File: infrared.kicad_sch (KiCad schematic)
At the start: 0 parts

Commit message: add TSOP75338TR library
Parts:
- added IC1: TSOP75338TR, TSOP75338TR:TSOP75338TR, symbol TSOP75338TR:TSOP75338TR
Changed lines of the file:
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@@
 	(generator_version "9.0")
 	(paper "A4")
+	(symbol
+		(lib_id "TSOP75338TR:TSOP75338TR")
+		(at 87.63 68.58 0)
+		(unit 1)
+		(exclude_from_sim no)
+		(in_bom yes)
+		(on_board yes)
+		(dnp no)
+		(fields_autoplaced yes)
+		(property "Reference" "IC1"
+			(at 109.22 71.1199 0)
+			(effects
+				(font
+					(size 1.27 1.27)
+				)
+				(justify left)
+			)
+		)
+		(property "Value" "TSOP75338TR"
+			(at 109.22 73.6599 0)
+			(effects
+				(font
+					(size 1.27 1.27)
+				)
+				(justify left)
+			)
+		)
+		(property "Footprint" "TSOP75338TR:TSOP75338TR"
+			(at 109.22 163.5 0)
+			(effects
+				(font
+					(size 1.27 1.27)
+				)
+				(justify left top)
+				(hide yes)
+			)
+		)
+		(property "Datasheet" "http://www.vishay.com/docs/82495/tsop753.pdf"
+			(at 109.22 263.5 0)
+			(effects
+				(font
+					(size 1.27 1.27)
+				)
+				(justify left top)
+				(hide yes)
+			)
+		)
+		(property "Description" "Vishay TSOP75338TR, 38kHz IR Receiver, 950nm +/-50 , 45m Range, 2.5V - 5V, SMT, 6.8 x 3 x 3.2mm"
+			(at 87.63 68.58 0)
+			(effects
+				(font
+					(size 1.27 1.27)
+				)
+				(hide yes)
+			)
+		)
+		(property "Height" "3.35"
+			(at 109.22 463.5 0)
+			(effects
+				(font
+					(size 1.27 1.27)
+				)
+				(justify left top)
+				(hide yes)
+			)
+		)
+		(property "Manufacturer_Name" "Vishay"
+			(at 109.22 563.5 0)
+			(effects
+				(font
+					(size 1.27 1.27)
+				)
+				(justify left top)
+				(hide yes)
+			)
+		)
+		(property "Manufacturer_Part_Number" "TSOP75338TR"
+			(at 109.22 663.5 0)
+			(effects
+				(font
+					(size 1.27 1.27)
+				)
+				(justify left top)
+				(hide yes)
+			)
+		)
+		(property "Mouser Part Number" "78-TSOP75338TR"
+			(at 109.22 763.5 0)
+			(effects
+				(font
+					(size 1.27 1.27)
+				)
+				(justify left top)
+				(hide yes)
+			)
+		)
+		(property "Mouser Price/Stock" "https://www.mouser.co.uk/ProductDetail/Vishay-Semiconductors/TSOP75338TR?qs=OZzrG8p9eNh0IrZXKXgo8Q%3D%3D"
+			(at 109.22 863.5 0)
+			(effects
+				(font
+					(size 1.27 1.27)
+				)
+				(justify left top)
+				(hide yes)
+			)
+		)
+		(property "Arrow Part Number" "TSOP75338TR"
+			(at 109.22 963.5 0)
+			(effects
+				(font
+					(size 1.27 1.27)
+				)
+				(justify left top)
+				(hide yes)
+			)
+		)
+		(property "Arrow Price/Stock" "https://www.arrow.com/en/products/tsop75338tr/vishay?utm_currency=USD&region=nac"
+			(at 109.22 1063.5 0)
+			(effects
+				(font
+					(size 1.27 1.27)
+				)
+				(justify left top)
+				(hide yes)
+			)
+		)
+		(pin "2"
+		)
+		(pin "4"
+		)
+		(pin "3"
+		)
+		(pin "1"
+		)
+		(instances
+			(project ""
+				(path "/3130e1f2-bde1-4b12-bd54-0e1e50bd36da/4b0b0d5d-6833-4670-bedb-8ac2688b21e7"
+					(reference "IC1")
+					(unit 1)
+				)
+			)
+		)
+	)
 )

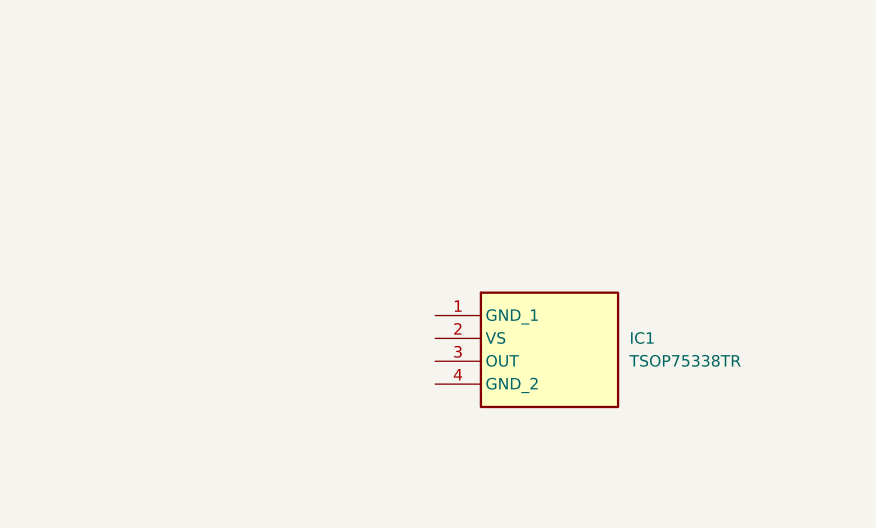
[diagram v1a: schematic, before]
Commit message: component placement inside schematic
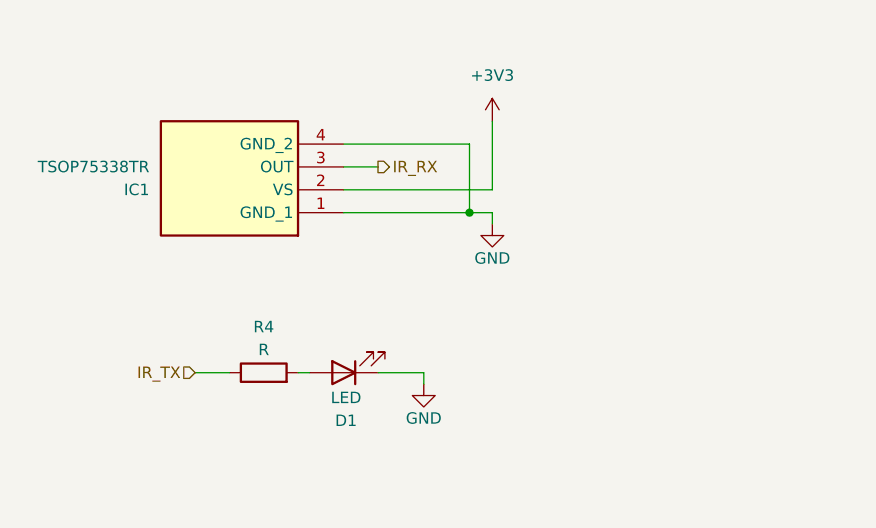
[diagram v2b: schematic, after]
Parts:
- added D1: LED, symbol Device:LED
- added R4: R, symbol Device:R
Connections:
- net GND: now reaches IC1.1 (GND_1)
- net GND: now also IC1.4 (GND_2), D1.1 (K)
- net +3V3: now reaches IC1.2 (VS)
- net IR_RX: now reaches IC1.3 (OUT)
- new net: D1.2 (A), R4.2
- new net IR_TX: R4.1
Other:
- moved on the sheet: IC1

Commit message: add external gpio connector
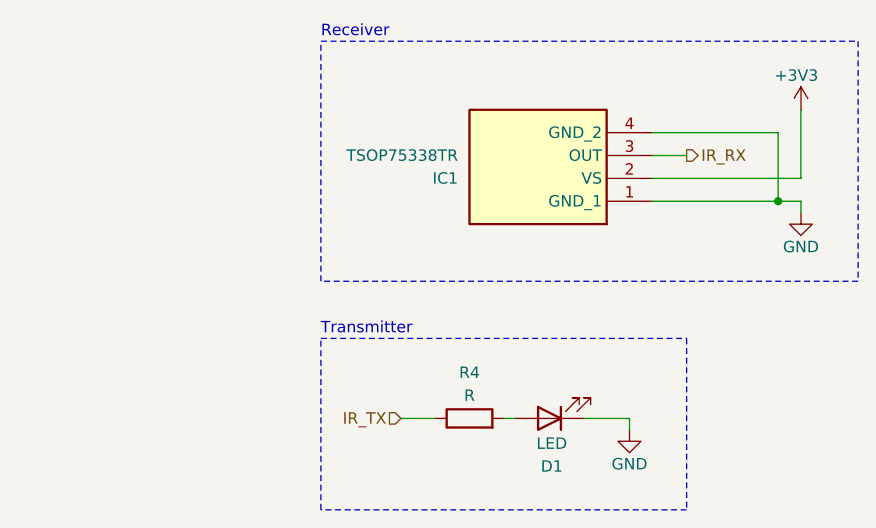
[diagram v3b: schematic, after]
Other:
- note added: "Receiver"
- note added: "Transmitter"
- moved on the sheet: D1, IC1, R4

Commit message: set initial component footprints
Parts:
- R11: renamed from R4; footprint (none) -> Resistor_SMD:R_0603_1608Metric
- renumbered D1 to D4, IC1 to IC2
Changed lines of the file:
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@@
 		(on_board yes)
 		(dnp no)
-		(property "Reference" "D1"
+		(property "Reference" "D4"
 			(at 100.584 85.344 0)
 			(effects
@@
 			(project ""
 				(path "/3130e1f2-bde1-4b12-bd54-0e1e50bd36da/4b0b0d5d-6833-4670-bedb-8ac2688b21e7"
-					(reference "D1")
+					(reference "D4")
 					(unit 1)
 				)
@@
 		(on_board yes)
 		(dnp no)
-		(property "Reference" "R4"
+		(property "Reference" "R11"
 			(at 91.44 74.93 90)
 			(effects
@@
 			)
 		)
-		(property "Footprint" ""
+		(property "Footprint" "Resistor_SMD:R_0603_1608Metric"
 			(at 91.44 81.788 90)
 			(effects
@@
 			(project ""
 				(path "/3130e1f2-bde1-4b12-bd54-0e1e50bd36da/4b0b0d5d-6833-4670-bedb-8ac2688b21e7"
-					(reference "R4")
+					(reference "R11")
 					(unit 1)
 				)
@@
 		(dnp no)
 		(fields_autoplaced yes)
-		(property "Reference" "IC1"
+		(property "Reference" "IC2"
 			(at 90.17 53.3401 0)
 			(effects
@@
 			(project ""
 				(path "/3130e1f2-bde1-4b12-bd54-0e1e50bd36da/4b0b0d5d-6833-4670-bedb-8ac2688b21e7"
-					(reference "IC1")
+					(reference "IC2")
 					(unit 1)
 				)
@@
 		(on_board yes)
 		(dnp no)
-		(property "Reference" "#PWR025"
+		(property "Reference" "#PWR017"
 			(at 128.27 49.53 0)
 			(effects
@@
 			(project ""
 				(path "/3130e1f2-bde1-4b12-bd54-0e1e50bd36da/4b0b0d5d-6833-4670-bedb-8ac2688b21e7"
-					(reference "#PWR025")
+					(reference "#PWR017")
 					(unit 1)
 				)
@@
 		(on_board yes)
 		(dnp no)
-		(property "Reference" "#PWR026"
+		(property "Reference" "#PWR018"
 			(at 128.27 63.5 0)
 			(effects
@@
 			(project ""
 				(path "/3130e1f2-bde1-4b12-bd54-0e1e50bd36da/4b0b0d5d-6833-4670-bedb-8ac2688b21e7"
-					(reference "#PWR026")
+					(reference "#PWR018")
 					(unit 1)
 				)
@@
 		(on_board yes)
 		(dnp no)
-		(property "Reference" "#PWR027"
+		(property "Reference" "#PWR016"
 			(at 109.22 87.63 0)
 			(effects
@@
 			(project ""
 				(path "/3130e1f2-bde1-4b12-bd54-0e1e50bd36da/4b0b0d5d-6833-4670-bedb-8ac2688b21e7"
-					(reference "#PWR027")
-					(unit 1)
-				)
+					(reference "#PWR016")
+					(unit 1)
+				)

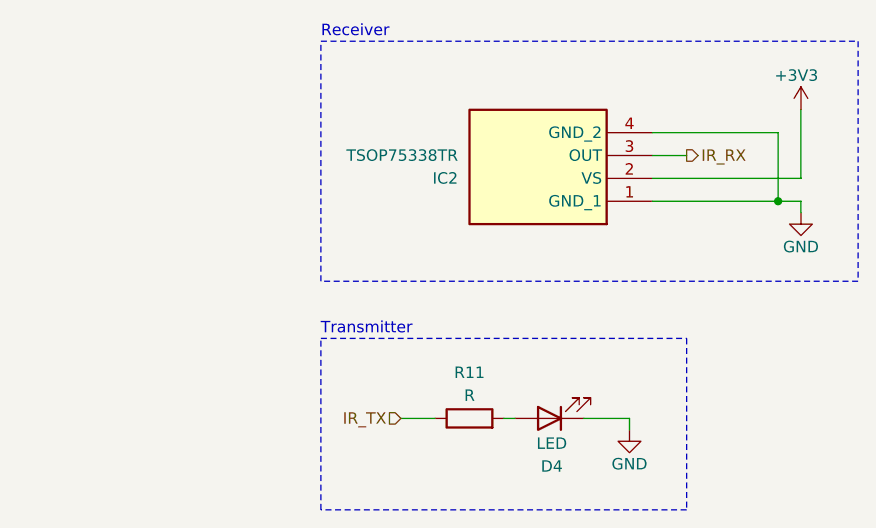
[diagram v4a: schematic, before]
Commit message: Add footprints
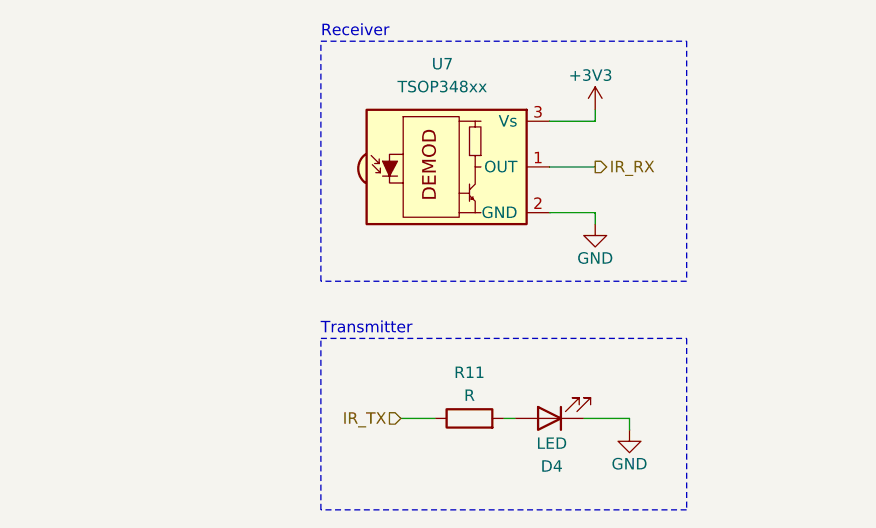
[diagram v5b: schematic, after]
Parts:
- removed IC2: TSOP75338TR, TSOP75338TR:TSOP75338TR, symbol TSOP75338TR:TSOP75338TR
- added U7: TSOP348xx, OptoDevice:Vishay_MOLD-3Pin, symbol Interface_Optical:TSOP348xx
- D4: footprint (none) -> LED_THT:LED_D3.0mm_Horizontal_O1.27mm_Z2.0mm
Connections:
- net +3V3: now also U7.3 (Vs)
- net GND: now also U7.2 (GND)
- net IR_RX: now also U7.1 (OUT)
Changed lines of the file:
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@@
 	(rectangle
 		(start 74.93 38.1)
-		(end 134.62 64.77)
+		(end 115.57 64.77)
 		(stroke
 			(width 0)
@@
 		)
 	)
-	(junction
-		(at 125.73 55.88)
-		(diameter 0)
-		(color 0 0 0 0)
-	)
 	(wire
 		(pts
@@
 	(wire
 		(pts
-			(xy 128.27 45.72) (xy 128.27 53.34)
-		)
-		(stroke
-			(width 0)
-			(type default)
-		)
-	)
-	(wire
-		(pts
-			(xy 125.73 48.26) (xy 111.76 48.26)
-		)
-		(stroke
-			(width 0)
-			(type default)
-		)
-	)
-	(wire
-		(pts
-			(xy 128.27 55.88) (xy 128.27 57.15)
+			(xy 105.41 45.72) (xy 105.41 46.99)
+		)
+		(stroke
+			(width 0)
+			(type default)
+		)
+	)
+	(wire
+		(pts
+			(xy 100.33 52.07) (xy 105.41 52.07)
+		)
+		(stroke
+			(width 0)
+			(type default)
+		)
+	)
+	(wire
+		(pts
+			(xy 105.41 57.15) (xy 105.41 58.42)
 		)
 		(stroke
@@
 	(wire
 		(pts
-			(xy 125.73 55.88) (xy 111.76 55.88)
-		)
-		(stroke
-			(width 0)
-			(type default)
-		)
-	)
-	(wire
-		(pts
-			(xy 128.27 53.34) (xy 111.76 53.34)
-		)
-		(stroke
-			(width 0)
-			(type default)
-		)
-	)
-	(wire
-		(pts
-			(xy 111.76 50.8) (xy 115.57 50.8)
-		)
-		(stroke
-			(width 0)
-			(type default)
-		)
-	)
-	(wire
-		(pts
-			(xy 125.73 48.26) (xy 125.73 55.88)
-		)
-		(stroke
-			(width 0)
-			(type default)
-		)
-	)
-	(wire
-		(pts
-			(xy 128.27 55.88) (xy 125.73 55.88)
+			(xy 100.33 57.15) (xy 105.41 57.15)
+		)
+		(stroke
+			(width 0)
+			(type default)
+		)
+	)
+	(wire
+		(pts
+			(xy 105.41 46.99) (xy 100.33 46.99)
 		)
 		(stroke
@@
 	(hierarchical_label "IR_RX"
 		(shape output)
-		(at 115.57 50.8 0)
+		(at 105.41 52.07 0)
 		(effects
 			(font
@@
 			)
 		)
-		(property "Footprint" ""
+		(property "Footprint" "LED_THT:LED_D3.0mm_Horizontal_O1.27mm_Z2.0mm"
 			(at 100.33 80.01 0)
 			(effects
@@
 	)
 	(symbol
+		(lib_id "Interface_Optical:TSOP348xx")
+		(at 90.17 52.07 0)
+		(unit 1)
+		(exclude_from_sim no)
+		(in_bom yes)
+		(on_board yes)
+		(dnp no)
+		(fields_autoplaced yes)
+		(property "Reference" "U7"
+			(at 88.435 40.64 0)
+			(effects
+				(font
+					(size 1.27 1.27)
+				)
+			)
+		)
+		(property "Value" "TSOP348xx"
+			(at 88.435 43.18 0)
+			(effects
+				(font
+					(size 1.27 1.27)
+				)
+			)
+		)
+		(property "Footprint" "OptoDevice:Vishay_MOLD-3Pin"
+			(at 88.9 61.595 0)
+			(effects
+				(font
+					(size 1.27 1.27)
+				)
+				(hide yes)
+			)
+		)
+		(property "Datasheet" "https://www.vishay.com/docs/82489/tsop322.pdf"
+			(at 106.68 44.45 0)
+			(effects
+				(font
+					(size 1.27 1.27)
+				)
+				(hide yes)
+			)
+		)
+		(property "Description" "IR Receiver Modules for Remote Control Systems"
+			(at 90.17 52.07 0)
+			(effects
+				(font
+					(size 1.27 1.27)
+				)
+				(hide yes)
+			)
+		)
+		(pin "2"
+		)
+		(pin "3"
+		)
+		(pin "1"
+		)
+		(instances
+			(project ""
+				(path "/3130e1f2-bde1-4b12-bd54-0e1e50bd36da/4b0b0d5d-6833-4670-bedb-8ac2688b21e7"
+					(reference "U7")
+					(unit 1)
+				)
+			)
+		)
+	)
+	(symbol
 		(lib_id "Device:R")
 		(at 91.44 80.01 90)
@@
 	)
 	(symbol
-		(lib_id "TSOP75338TR:TSOP75338TR")
-		(at 111.76 55.88 180)
-		(unit 1)
-		(exclude_from_sim no)
-		(in_bom yes)
-		(on_board yes)
-		(dnp no)
-		(fields_autoplaced yes)
-		(property "Reference" "IC2"
-			(at 90.17 53.3401 0)
-			(effects
-				(font
-					(size 1.27 1.27)
-				)
-				(justify left)
-			)
-		)
-		(property "Value" "TSOP75338TR"
-			(at 90.17 50.8001 0)
-			(effects
-				(font
-					(size 1.27 1.27)
-				)
-				(justify left)
-			)
-		)
-		(property "Footprint" "TSOP75338TR:TSOP75338TR"
-			(at 90.17 -39.04 0)
-			(effects
-				(font
-					(size 1.27 1.27)
-				)
-				(justify left top)
-				(hide yes)
-			)
-		)
-		(property "Datasheet" "http://www.vishay.com/docs/82495/tsop753.pdf"
-			(at 90.17 -139.04 0)
-			(effects
-				(font
-					(size 1.27 1.27)
-				)
-				(justify left top)
-				(hide yes)
-			)
-		)
-		(property "Description" "Vishay TSOP75338TR, 38kHz IR Receiver, 950nm +/-50 , 45m Range, 2.5V - 5V, SMT, 6.8 x 3 x 3.2mm"
-			(at 111.76 55.88 0)
-			(effects
-				(font
-					(size 1.27 1.27)
-				)
-				(hide yes)
-			)
-		)
-		(property "Height" "3.35"
-			(at 90.17 -339.04 0)
-			(effects
-				(font
-					(size 1.27 1.27)
-				)
-				(justify left top)
-				(hide yes)
-			)
-		)
-		(property "Manufacturer_Name" "Vishay"
-			(at 90.17 -439.04 0)
-			(effects
-				(font
-					(size 1.27 1.27)
-				)
-				(justify left top)
-				(hide yes)
-			)
-		)
-		(property "Manufacturer_Part_Number" "TSOP75338TR"
-			(at 90.17 -539.04 0)
-			(effects
-				(font
-					(size 1.27 1.27)
-				)
-				(justify left top)
-				(hide yes)
-			)
-		)
-		(property "Mouser Part Number" "78-TSOP75338TR"
-			(at 90.17 -639.04 0)
-			(effects
-				(font
-					(size 1.27 1.27)
-				)
-				(justify left top)
-				(hide yes)
-			)
-		)
-		(property "Mouser Price/Stock" "https://www.mouser.co.uk/ProductDetail/Vishay-Semiconductors/TSOP75338TR?qs=OZzrG8p9eNh0IrZXKXgo8Q%3D%3D"
-			(at 90.17 -739.04 0)
-			(effects
-				(font
-					(size 1.27 1.27)
-				)
-				(justify left top)
-				(hide yes)
-			)
-		)
-		(property "Arrow Part Number" "TSOP75338TR"
-			(at 90.17 -839.04 0)
-			(effects
-				(font
-					(size 1.27 1.27)
-				)
-				(justify left top)
-				(hide yes)
-			)
-		)
-		(property "Arrow Price/Stock" "https://www.arrow.com/en/products/tsop75338tr/vishay?utm_currency=USD&region=nac"
-			(at 90.17 -939.04 0)
-			(effects
-				(font
-					(size 1.27 1.27)
-				)
-				(justify left top)
-				(hide yes)
-			)
-		)
-		(pin "2"
-		)
-		(pin "4"
-		)
-		(pin "3"
-		)
-		(pin "1"
-		)
-		(instances
-			(project ""
-				(path "/3130e1f2-bde1-4b12-bd54-0e1e50bd36da/4b0b0d5d-6833-4670-bedb-8ac2688b21e7"
-					(reference "IC2")
-					(unit 1)
-				)
-			)
-		)
-	)
-	(symbol
 		(lib_id "power:+3V3")
-		(at 128.27 45.72 0)
+		(at 105.41 45.72 0)
 		(unit 1)
 		(exclude_from_sim no)
@@
 		(dnp no)
 		(property "Reference" "#PWR017"
-			(at 128.27 49.53 0)
+			(at 105.41 49.53 0)
 			(effects
 				(font
@@
 		)
 		(property "Value" "+3V3"
-			(at 127.762 41.91 0)
+			(at 104.902 41.91 0)
 			(effects
 				(font
@@
 		)
 		(property "Footprint" ""
-			(at 128.27 45.72 0)
+			(at 105.41 45.72 0)
 			(effects
 				(font
@@
 		)
 		(property "Datasheet" ""
-			(at 128.27 45.72 0)
+			(at 105.41 45.72 0)
 			(effects
 				(font
@@
 		)
 		(property "Description" "Power symbol creates a global label with name \"+3V3\""
-			(at 128.27 45.72 0)
+			(at 105.41 45.72 0)
 			(effects
 				(font
@@
 	(symbol
 		(lib_id "power:GND")
-		(at 128.27 57.15 0)
+		(at 105.41 58.42 0)
 		(unit 1)
 		(exclude_from_sim no)
@@
 		(dnp no)
 		(property "Reference" "#PWR018"
-			(at 128.27 63.5 0)
+			(at 105.41 64.77 0)
 			(effects
 				(font
@@
 		)
 		(property "Value" "GND"
-			(at 128.27 60.96 0)
+			(at 105.41 62.23 0)
 			(effects
 				(font
@@
 		)
 		(property "Footprint" ""
-			(at 128.27 57.15 0)
+			(at 105.41 58.42 0)
 			(effects
 				(font
@@
 		)
 		(property "Datasheet" ""
-			(at 128.27 57.15 0)
+			(at 105.41 58.42 0)
 			(effects
 				(font
@@
 		)
 		(property "Description" "Power symbol creates a global label with name \"GND\" , ground"
-			(at 128.27 57.15 0)
-			(effects
-				(font
+			(at 105.41 58.42 0)
+			(effects
+				(font

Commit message: modify ios
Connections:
- net +3V3: now also D4.2 (A)
- net GND: no longer D4.1 (K)
- net at R11.2: now also D4.1 (K); no longer D4.2 (A)
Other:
- moved on the sheet: D4
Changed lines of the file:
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@@
-	(wire
-		(pts
-			(xy 109.22 80.01) (xy 109.22 81.28)
-		)
-		(stroke
-			(width 0)
-			(type default)
-		)
-	)
 	(wire
 		(pts
@@
 		(pts
 			(xy 105.41 46.99) (xy 100.33 46.99)
+		)
+		(stroke
+			(width 0)
+			(type default)
+		)
+	)
+	(wire
+		(pts
+			(xy 109.22 78.74) (xy 109.22 80.01)
 		)
 		(stroke
@@
 	(symbol
 		(lib_id "Device:LED")
-		(at 100.33 80.01 180)
+		(at 100.33 80.01 0)
 		(unit 1)
 		(exclude_from_sim no)
@@
 		(dnp no)
 		(property "Reference" "D4"
-			(at 100.584 85.344 0)
+			(at 100.076 74.676 0)
 			(effects
 				(font
@@
 		)
 		(property "Value" "LED"
-			(at 100.584 82.804 0)
+			(at 100.076 77.216 0)
 			(effects
 				(font
@@
 	(symbol
 		(lib_id "power:+3V3")
+		(at 109.22 78.74 0)
+		(unit 1)
+		(exclude_from_sim no)
+		(in_bom yes)
+		(on_board yes)
+		(dnp no)
+		(fields_autoplaced yes)
+		(property "Reference" "#PWR016"
+			(at 109.22 82.55 0)
+			(effects
+				(font
+					(size 1.27 1.27)
+				)
+				(hide yes)
+			)
+		)
+		(property "Value" "+3V3"
+			(at 109.22 73.66 0)
+			(effects
+				(font
+					(size 1.27 1.27)
+				)
+			)
+		)
+		(property "Footprint" ""
+			(at 109.22 78.74 0)
+			(effects
+				(font
+					(size 1.27 1.27)
+				)
+				(hide yes)
+			)
+		)
+		(property "Datasheet" ""
+			(at 109.22 78.74 0)
+			(effects
+				(font
+					(size 1.27 1.27)
+				)
+				(hide yes)
+			)
+		)
+		(property "Description" "Power symbol creates a global label with name \"+3V3\""
+			(at 109.22 78.74 0)
+			(effects
+				(font
+					(size 1.27 1.27)
+				)
+				(hide yes)
+			)
+		)
+		(pin "1"
+		)
+		(instances
+			(project ""
+				(path "/3130e1f2-bde1-4b12-bd54-0e1e50bd36da/4b0b0d5d-6833-4670-bedb-8ac2688b21e7"
+					(reference "#PWR016")
+					(unit 1)
+				)
+			)
+		)
+	)
+	(symbol
+		(lib_id "power:+3V3")
 		(at 105.41 45.72 0)
 		(unit 1)
@@
 					(unit 1)
 				)
-			)
-		)
-	)
-	(symbol
-		(lib_id "power:GND")
-		(at 109.22 81.28 0)
-		(unit 1)
-		(exclude_from_sim no)
-		(in_bom yes)
-		(on_board yes)
-		(dnp no)
-		(property "Reference" "#PWR016"
-			(at 109.22 87.63 0)
-			(effects
-				(font
-					(size 1.27 1.27)
-				)
-				(hide yes)
-			)
-		)
-		(property "Value" "GND"
-			(at 109.22 85.09 0)
-			(effects
-				(font
-					(size 1.27 1.27)
-				)
-			)
-		)
-		(property "Footprint" ""
-			(at 109.22 81.28 0)
-			(effects
-				(font
-					(size 1.27 1.27)
-				)
-				(hide yes)
-			)
-		)
-		(property "Datasheet" ""
-			(at 109.22 81.28 0)
-			(effects
-				(font
-					(size 1.27 1.27)
-				)
-				(hide yes)
-			)
-		)
-		(property "Description" "Power symbol creates a global label with name \"GND\" , ground"
-			(at 109.22 81.28 0)
-			(effects
-				(font
-					(size 1.27 1.27)
-				)
-				(hide yes)
-			)
-		)
-		(pin "1"
-		)
-		(instances
-			(project ""
-				(path "/3130e1f2-bde1-4b12-bd54-0e1e50bd36da/4b0b0d5d-6833-4670-bedb-8ac2688b21e7"
-					(reference "#PWR016")
-					(unit 1)
-				)

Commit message: LUIGI
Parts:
- R11: value R -> 100R
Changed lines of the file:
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@@
 			)
 		)
-		(property "Value" "R"
+		(property "Value" "100R"
 			(at 91.44 77.47 90)
 			(effects
